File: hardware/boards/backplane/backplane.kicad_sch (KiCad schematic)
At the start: 0 parts

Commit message: Add backplane power connector schematic
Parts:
- added J1: DC_IN_SCREW_TERMINAL, TerminalBlock_Phoenix:TerminalBlock_Phoenix_MKDS-1,5-2-5.08_1x02_P5.08mm_Horizontal, symbol Connector_Generic:Conn_01x02
- added J2: XT30U(2+2)-F.G.B_SLOT1, mini-rack-power:Amass_XT30U_2plus2_F_RightAngle_Mechanical, symbol Connector_Generic:Conn_01x04
- added J3: XT30U(2+2)-F.G.B_SLOT2, mini-rack-power:Amass_XT30U_2plus2_F_RightAngle_Mechanical, symbol Connector_Generic:Conn_01x04
- added J4: XT30U(2+2)-F.G.B_SLOT3, mini-rack-power:Amass_XT30U_2plus2_F_RightAngle_Mechanical, symbol Connector_Generic:Conn_01x04
- added J5: XT30U(2+2)-F.G.B_SLOT4, mini-rack-power:Amass_XT30U_2plus2_F_RightAngle_Mechanical, symbol Connector_Generic:Conn_01x04
- added J6: XT30U(2+2)-F.G.B_SLOT5, mini-rack-power:Amass_XT30U_2plus2_F_RightAngle_Mechanical, symbol Connector_Generic:Conn_01x04
- added J7: XT30U(2+2)-F.G.B_SLOT6, mini-rack-power:Amass_XT30U_2plus2_F_RightAngle_Mechanical, symbol Connector_Generic:Conn_01x04
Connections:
- new net DC_IN+: J1.1 (Pin_1), J2.1 (Pin_1), J3.1 (Pin_1), J4.1 (Pin_1), J5.1 (Pin_1), J6.1 (Pin_1), J7.1 (Pin_1)
- new net GND: J1.2 (Pin_2), J2.2 (Pin_2), J3.2 (Pin_2), J4.2 (Pin_2), J5.2 (Pin_2), J6.2 (Pin_2), J7.2 (Pin_2)
- new net SLOT1_SCL: J2.4 (Pin_4)
- new net SLOT1_SDA: J2.3 (Pin_3)
- new net SLOT2_SCL: J3.4 (Pin_4)
- new net SLOT2_SDA: J3.3 (Pin_3)
- new net SLOT3_SCL: J4.4 (Pin_4)
- new net SLOT3_SDA: J4.3 (Pin_3)
- new net SLOT4_SCL: J5.4 (Pin_4)
- new net SLOT4_SDA: J5.3 (Pin_3)
- new net SLOT5_SCL: J6.4 (Pin_4)
- new net SLOT5_SDA: J6.3 (Pin_3)
- new net SLOT6_SCL: J7.4 (Pin_4)
- new net SLOT6_SDA: J7.3 (Pin_3)
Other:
- note added: "XT30 pin assumption: 1=DC_IN+, 2=GND, 3=SDA, 4=SCL. Verify XT30U female electrical footprint before PCB layout."

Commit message: Checkpoint
_sigh_
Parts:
- added C1: 100nF, Capacitor_SMD:C_0603_1608Metric, symbol Device:C
- added JP1: A0_ADDR, Jumper:SolderJumper-3_P1.3mm_Bridged12_Pad1.0x1.5mm, symbol Jumper:SolderJumper_3_Bridged12
- added JP2: A1_ADDR, Jumper:SolderJumper-3_P1.3mm_Bridged12_Pad1.0x1.5mm, symbol Jumper:SolderJumper_3_Bridged12
- added JP3: A2_ADDR, Jumper:SolderJumper-3_P1.3mm_Bridged12_Pad1.0x1.5mm, symbol Jumper:SolderJumper_3_Bridged12
- added R1: 10k, Resistor_SMD:R_0603_1608Metric, symbol Device:R
- added U1: TCA9548APWR, Package_SO:TSSOP-24_4.4x7.8mm_P0.65mm, symbol Interface_Expansion:TCA9548APWR
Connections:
- net GND: now also C1.2, JP1.1 (A), JP2.1 (A), JP3.1 (A), U1.12 (GND)
- net SLOT1_SCL renamed SCL_SLOT_1
- net SCL_SLOT_1: now also U1.5 (SC0)
- net SLOT1_SDA renamed SDA_SLOT_1
- net SDA_SLOT_1: now also U1.4 (SD0)
- net SLOT2_SCL renamed SCL_SLOT_2
- net SCL_SLOT_2: now also U1.7 (SC1)
- net SLOT2_SDA renamed SDA_SLOT_2
- net SDA_SLOT_2: now also U1.6 (SD1)
- net SLOT3_SCL renamed SCL_SLOT_3
- net SCL_SLOT_3: now also U1.9 (SC2)
- net SLOT3_SDA renamed SDA_SLOT_3
- net SDA_SLOT_3: now also U1.8 (SD2)
- net SLOT4_SCL renamed SCL_SLOT_4
- net SCL_SLOT_4: now also U1.11 (SC3)
- net SLOT4_SDA renamed SDA_SLOT_4
- net SDA_SLOT_4: now also U1.10 (SD3)
- net SLOT5_SCL renamed SCL_SLOT_5
- net SCL_SLOT_5: now also U1.14 (SC4)
- net SLOT5_SDA renamed SDA_SLOT_5
- net SDA_SLOT_5: now also U1.13 (SD4)
- net SLOT6_SCL renamed SCL_SLOT_6
- net SCL_SLOT_6: now also U1.16 (SC5)
- net SLOT6_SDA renamed SDA_SLOT_6
- net SDA_SLOT_6: now also U1.15 (SD5)
- new net: R1.2, U1.3 (~{RESET})
- new net +3V3: C1.1, JP1.3 (B), JP2.3 (B), JP3.3 (B), R1.1, U1.24 (VCC)
- new net I2C_UP_SCL: U1.22 (SCL)
- new net I2C_UP_SDA: U1.23 (SDA)
- new net TCA9548A_A0: JP1.2 (C), U1.1 (A0)
- new net TCA9548A_A1: JP2.2 (C), U1.2 (A1)
- new net TCA9548A_A2: JP3.2 (C), U1.21 (A2)
- no-connect marks 0 -> 4
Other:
- note added: "TCA9548A: JP1-JP3 default A0/A1/A2 low for 0x70; cut 1-2 and bridge 1-3 to set a bit high. VCC_I2C rail and I2C pull-up placement/value still TBD."

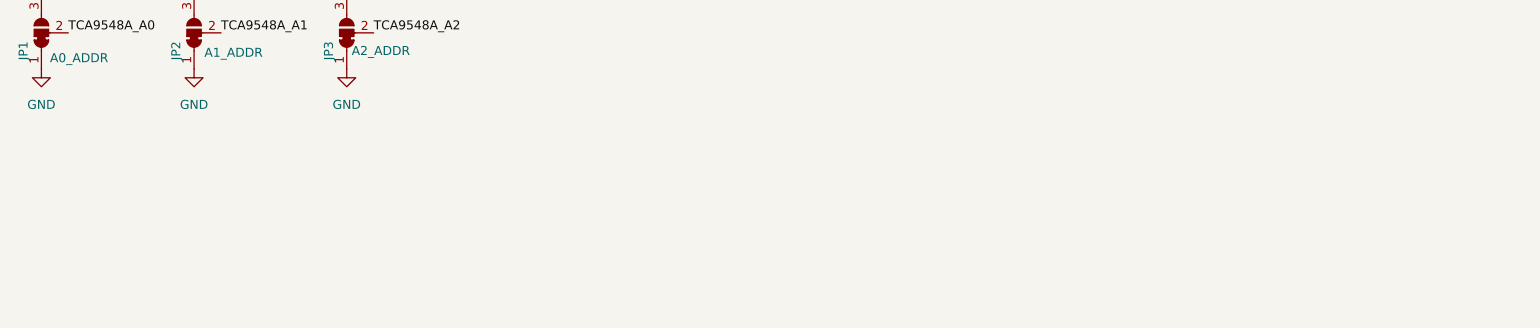
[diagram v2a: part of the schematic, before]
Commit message: Add backplane slot LED indicators
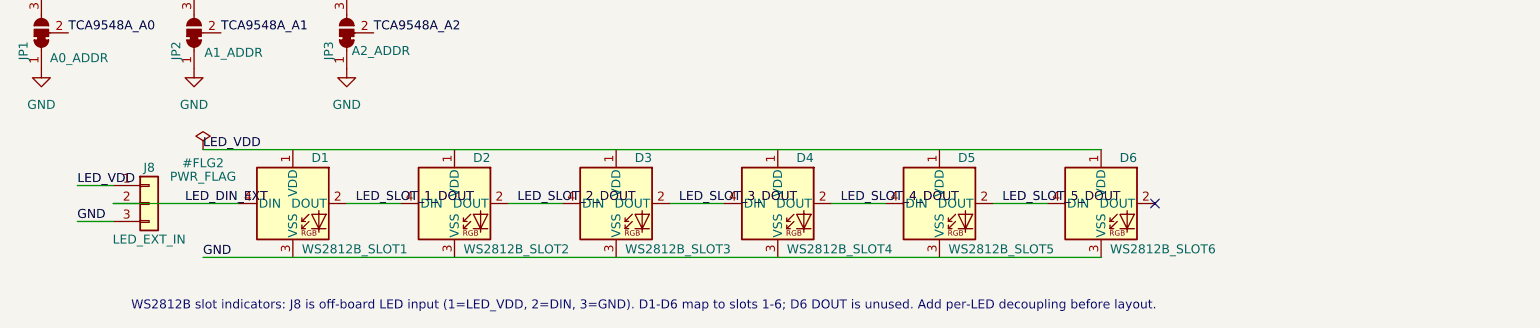
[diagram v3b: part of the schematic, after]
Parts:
- added D1: WS2812B_SLOT1, LED_SMD:LED_WS2812B_PLCC4_5.0x5.0mm_P3.2mm, symbol LED:WS2812B
- added D2: WS2812B_SLOT2, LED_SMD:LED_WS2812B_PLCC4_5.0x5.0mm_P3.2mm, symbol LED:WS2812B
- added D3: WS2812B_SLOT3, LED_SMD:LED_WS2812B_PLCC4_5.0x5.0mm_P3.2mm, symbol LED:WS2812B
- added D4: WS2812B_SLOT4, LED_SMD:LED_WS2812B_PLCC4_5.0x5.0mm_P3.2mm, symbol LED:WS2812B
- added D5: WS2812B_SLOT5, LED_SMD:LED_WS2812B_PLCC4_5.0x5.0mm_P3.2mm, symbol LED:WS2812B
- added D6: WS2812B_SLOT6, LED_SMD:LED_WS2812B_PLCC4_5.0x5.0mm_P3.2mm, symbol LED:WS2812B
- added J8: LED_EXT_IN, Connector_PinHeader_2.54mm:PinHeader_1x03_P2.54mm_Vertical, symbol Connector_Generic:Conn_01x03
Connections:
- net GND: now also D1.3 (VSS), D2.3 (VSS), D3.3 (VSS), D4.3 (VSS), D5.3 (VSS), D6.3 (VSS), J8.3 (Pin_3)
- new net LED_DIN_EXT: D1.4 (DIN), J8.2 (Pin_2)
- new net LED_SLOT_1_DOUT: D1.2 (DOUT), D2.4 (DIN)
- new net LED_SLOT_2_DOUT: D2.2 (DOUT), D3.4 (DIN)
- new net LED_SLOT_3_DOUT: D3.2 (DOUT), D4.4 (DIN)
- new net LED_SLOT_4_DOUT: D4.2 (DOUT), D5.4 (DIN)
- new net LED_SLOT_5_DOUT: D5.2 (DOUT), D6.4 (DIN)
- new net LED_VDD: D1.1 (VDD), D2.1 (VDD), D3.1 (VDD), D4.1 (VDD), D5.1 (VDD), D6.1 (VDD), J8.1 (Pin_1)
- no-connect marks 4 -> 5
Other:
- note added: "WS2812B slot indicators: J8 is off-board LED input (1=LED_VDD, 2=DIN, 3=GND). D1-D6 map to slots 1-6; D6 DOUT is unused. Add per-LED decoupling before layout."

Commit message: Add backplane I2C protection and chaining connectors
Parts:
- added D10, D11, D12, D13, D14, D15, D16, D17, D18, D7, D8, D9: LOW_CAP_TVS, Diode_SMD:D_SOD-523, symbol Device:D_TVS
- added J10: I2C_CHAIN_IN, Connector_PinHeader_2.54mm:PinHeader_1x04_P2.54mm_Vertical, symbol Connector_Generic:Conn_01x04
- added J11: I2C_CHAIN_OUT, Connector_PinHeader_2.54mm:PinHeader_1x04_P2.54mm_Vertical, symbol Connector_Generic:Conn_01x04
- added J12: LED_EXT_OUT, Connector_PinHeader_2.54mm:PinHeader_1x03_P2.54mm_Vertical, symbol Connector_Generic:Conn_01x03
- added J9: DC_CHAIN_OUT, TerminalBlock_Phoenix:TerminalBlock_Phoenix_MKDS-1,5-2-5.08_1x02_P5.08mm_Horizontal, symbol Connector_Generic:Conn_01x02
- added R10, R11, R12, R13, R2, R3, R4, R5, R6, R7, R8, R9: 47R, Resistor_SMD:R_0603_1608Metric, symbol Device:R
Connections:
- net +3V3: now also J10.4 (Pin_4), J11.4 (Pin_4)
- net DC_IN+: now also J9.1 (Pin_1)
- net GND: now also D10.2 (A2), D11.2 (A2), D12.2 (A2), D13.2 (A2), D14.2 (A2), D15.2 (A2), D16.2 (A2), D17.2 (A2), D18.2 (A2), D7.2 (A2), D8.2 (A2), D9.2 (A2), J10.1 (Pin_1), J11.1 (Pin_1), J12.3 (Pin_3), J9.2 (Pin_2)
- net I2C_UP_SCL: now also J10.3 (Pin_3), J11.3 (Pin_3)
- net I2C_UP_SDA: now also J10.2 (Pin_2), J11.2 (Pin_2)
- net LED_VDD: now also J12.1 (Pin_1)
- net SCL_SLOT_1: now also R3.2; no longer J2.4 (Pin_4)
- net SCL_SLOT_2: now also R5.2; no longer J3.4 (Pin_4)
- net SCL_SLOT_3: now also R7.2; no longer J4.4 (Pin_4)
- net SCL_SLOT_4: now also R9.2; no longer J5.4 (Pin_4)
- net SCL_SLOT_5: now also R11.2; no longer J6.4 (Pin_4)
- net SCL_SLOT_6: now also R13.2; no longer J7.4 (Pin_4)
- net SDA_SLOT_1: now also R2.2; no longer J2.3 (Pin_3)
- net SDA_SLOT_2: now also R4.2; no longer J3.3 (Pin_3)
- net SDA_SLOT_3: now also R6.2; no longer J4.3 (Pin_3)
- net SDA_SLOT_4: now also R8.2; no longer J5.3 (Pin_3)
- net SDA_SLOT_5: now also R10.2; no longer J6.3 (Pin_3)
- net SDA_SLOT_6: now also R12.2; no longer J7.3 (Pin_3)
- net LED_DOUT_EXT: now reaches D6.2 (DOUT)
- net LED_DOUT_EXT: now also J12.2 (Pin_2)
- new net SCL_SLOT_1_CONN: D8.1 (A1), J2.4 (Pin_4), R3.1
- new net SCL_SLOT_2_CONN: D10.1 (A1), J3.4 (Pin_4), R5.1
- new net SCL_SLOT_3_CONN: D12.1 (A1), J4.4 (Pin_4), R7.1
- new net SCL_SLOT_4_CONN: D14.1 (A1), J5.4 (Pin_4), R9.1
- new net SCL_SLOT_5_CONN: D16.1 (A1), J6.4 (Pin_4), R11.1
- new net SCL_SLOT_6_CONN: D18.1 (A1), J7.4 (Pin_4), R13.1
- new net SDA_SLOT_1_CONN: D7.1 (A1), J2.3 (Pin_3), R2.1
- new net SDA_SLOT_2_CONN: D9.1 (A1), J3.3 (Pin_3), R4.1
- new net SDA_SLOT_3_CONN: D11.1 (A1), J4.3 (Pin_3), R6.1
- new net SDA_SLOT_4_CONN: D13.1 (A1), J5.3 (Pin_3), R8.1
- new net SDA_SLOT_5_CONN: D15.1 (A1), J6.3 (Pin_3), R10.1
- new net SDA_SLOT_6_CONN: D17.1 (A1), J7.3 (Pin_3), R12.1
- no-connect marks 5 -> 4
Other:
- note added: "Daisy-chain connectors: J9 parallels J1 for DC. J10/J11 parallel the upstream I2C bus as GND/SDA/SCL/+3V3. J12 exports LED_VDD, D6 DOUT, and GND."
- note added: "Per-slot I2C hot-plug protection: R2-R13 are 47R series resistors. D7-D18 are low-cap TVS placeholders from connector-side nets to GND; final TVS capacitance/clamp TBD."
- note added: "WS2812B slot indicators: J8 is off-board LED input (1=LED_VDD, 2=DIN, 3=GND). D1-D6 map to slots 1-6; J12 exports D6 DOUT for daisy-chain output. Add per-LED decoupling before layout."
- note removed: "WS2812B slot indicators: J8 is off-board LED input (1=LED_VDD, 2=DIN, 3=GND). D1-D6 map to slots 1-6; D6 DOUT is unused. Add per-LED decoupling before layout."

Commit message: chore: add placeholder part source properties
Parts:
- C1, D1, D10, D11, D12, D13, D14, D15, D16, D17, D18, D2, D3, D4, D5, D6, D7, D8, D9, J1, J10, J11, J12, J2, J3, J4, J5, J6, J7, J8, J9, JP1, JP2, JP3, R1, R10, R11, R12, R13, R2, R3, R4, R5, R6, R7, R8, R9, U1: Part_source (none) -> LCSC,XXXXXXX

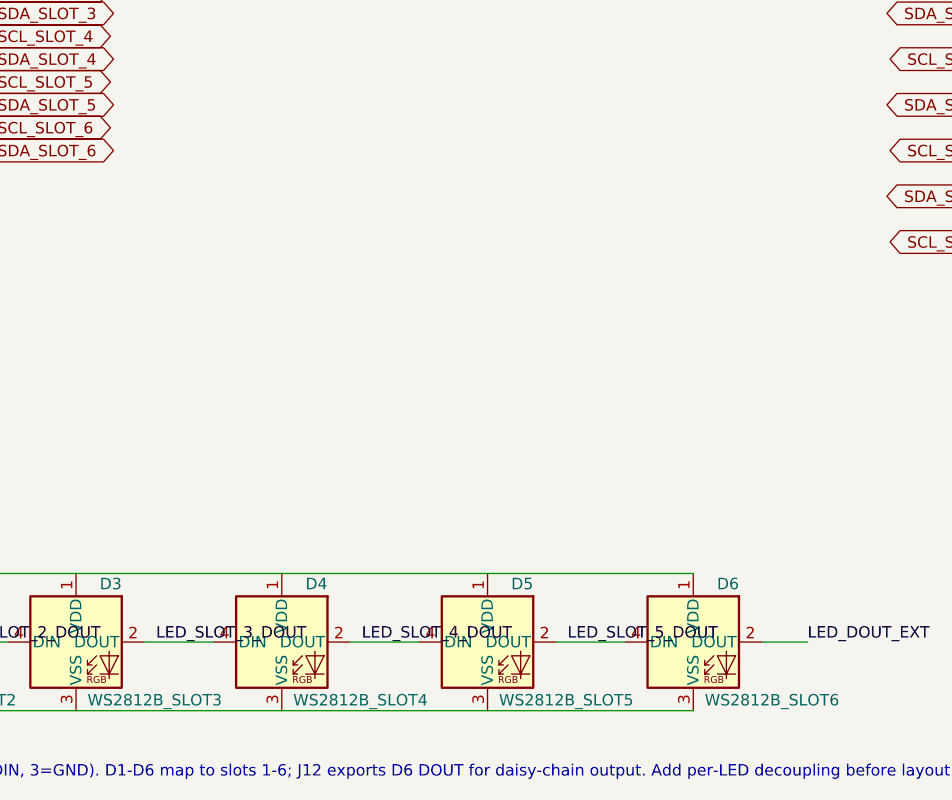
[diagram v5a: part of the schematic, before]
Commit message: add wt32 eth01 backplane module
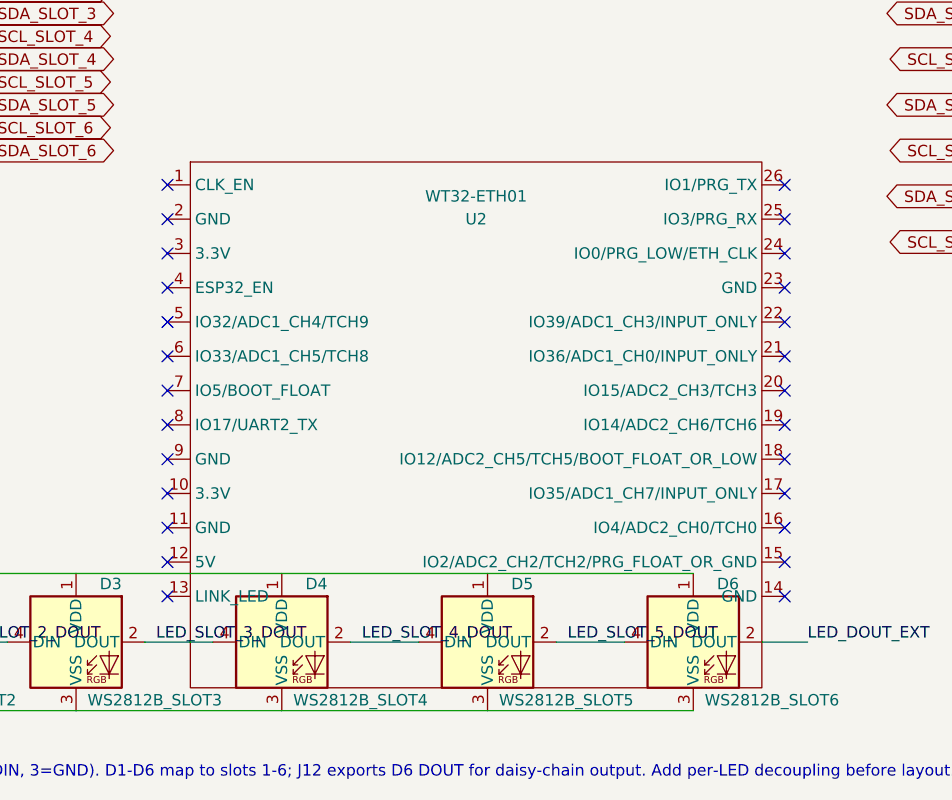
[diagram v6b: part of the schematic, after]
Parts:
- added U2: WT32-ETH01, WT32-ETH01:WT32-ETH01, symbol WT32-ETH01:WT32-ETH01
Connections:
- no-connect marks 4 -> 30
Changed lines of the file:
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@@
+		)
+	)
+	(no_connect
+		(at 114.30 151.13)
+	)
+	(no_connect
+		(at 114.30 185.42)
+	)
+	(no_connect
+		(at 114.30 189.23)
+	)
+	(no_connect
+		(at 114.30 193.04)
+	)
+	(no_connect
+		(at 114.30 196.85)
+	)
+	(no_connect
+		(at 182.88 196.85)
+	)
+	(no_connect
+		(at 182.88 193.04)
+	)
+	(no_connect
+		(at 182.88 189.23)
+	)
+	(no_connect
+		(at 182.88 185.42)
+	)
+	(no_connect
+		(at 182.88 181.61)
+	)
+	(no_connect
+		(at 182.88 177.80)
+	)
+	(no_connect
+		(at 114.30 154.94)
+	)
+	(no_connect
+		(at 182.88 173.99)
+	)
+	(no_connect
+		(at 182.88 170.18)
+	)
+	(no_connect
+		(at 182.88 166.37)
+	)
+	(no_connect
+		(at 182.88 162.56)
+	)
+	(no_connect
+		(at 182.88 158.75)
+	)
+	(no_connect
+		(at 182.88 154.94)
+	)
+	(no_connect
+		(at 182.88 151.13)
+	)
+	(no_connect
+		(at 114.30 158.75)
+	)
+	(no_connect
+		(at 114.30 162.56)
+	)
+	(no_connect
+		(at 114.30 166.37)
+	)
+	(no_connect
+		(at 114.30 170.18)
+	)
+	(no_connect
+		(at 114.30 173.99)
+	)
+	(no_connect
+		(at 114.30 177.80)
+	)
+	(no_connect
+		(at 114.30 181.61)
+	)
+	(symbol
+		(lib_id "WT32-ETH01:WT32-ETH01")
+		(at 148.59 177.80 0)
+		(unit 1)
+		(body_style 1)
+		(exclude_from_sim no)
+		(in_bom yes)
+		(on_board yes)
+		(in_pos_files yes)
+		(dnp no)
+		(property "Reference" "U2"
+			(at 148.59 154.94 0)
+			(show_name no)
+			(do_not_autoplace no)
+			(effects
+				(font
+					(size 1.27 1.27)
+				)
+			)
+		)
+		(property "Value" "WT32-ETH01"
+			(at 148.59 152.40 0)
+			(show_name no)
+			(do_not_autoplace no)
+			(effects
+				(font
+					(size 1.27 1.27)
+				)
+			)
+		)
+		(property "Footprint" "WT32-ETH01:WT32-ETH01"
+			(at 148.59 177.80 0)
+			(hide yes)
+			(show_name no)
+			(do_not_autoplace no)
+			(effects
+				(font
+					(size 1.27 1.27)
+				)
+			)
+		)
+		(property "Datasheet" "${KIPRJMOD}/../../libraries/vendor/wt32-eth01/WT32-ETH01-datasheet-v1.4-en.pdf"
+			(at 148.59 177.80 0)
+			(hide yes)
+			(show_name no)
+			(do_not_autoplace no)
+			(effects
+				(font
+					(size 1.27 1.27)
+				)
+			)
+		)
+		(property "Description" "WT32-ETH01 ESP32 Ethernet module"
+			(at 148.59 177.80 0)
+			(hide yes)
+			(show_name no)
+			(do_not_autoplace no)
+			(effects
+				(font
+					(size 1.27 1.27)
+				)
+			)
+		)
+		(property "Part_source" "LCSC,XXXXXXX"
+			(at 148.59 177.80 0)
+			(hide yes)
+			(show_name no)
+			(do_not_autoplace no)
+			(effects
+				(font
+					(size 1.27 1.27)
+				)
+			)
+		)
+		(pin "1"
+		)
+		(pin "10"
+		)
+		(pin "11"
+		)
+		(pin "12"
+		)
+		(pin "13"
+		)
+		(pin "14"
+		)
+		(pin "15"
+		)
+		(pin "16"
+		)
+		(pin "17"
+		)
+		(pin "18"
+		)
+		(pin "19"
+		)
+		(pin "2"
+		)
+		(pin "20"
+		)
+		(pin "21"
+		)
+		(pin "22"
+		)
+		(pin "23"
+		)
+		(pin "24"
+		)
+		(pin "25"
+		)
+		(pin "26"
+		)
+		(pin "3"
+		)
+		(pin "4"
+		)
+		(pin "5"
+		)
+		(pin "6"
+		)
+		(pin "7"
+		)
+		(pin "8"
+		)
+		(pin "9"
+		)
+		(instances
+			(project "backplane"
+				(path "/5e4f3adc-13b5-4625-8ac7-2a60909b6ea0"
+					(reference "U2")
+					(unit 1)
+				)
+			)
 		)
 	)

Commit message: Split backplane schematic pages
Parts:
- removed C1: 100nF, Capacitor_SMD:C_0603_1608Metric, symbol Device:C
- removed D1: WS2812B_SLOT1, LED_SMD:LED_WS2812B_PLCC4_5.0x5.0mm_P3.2mm, symbol LED:WS2812B
- removed D10, D11, D12, D13, D14, D15, D16, D17, D18, D7, D8, D9: LOW_CAP_TVS, Diode_SMD:D_SOD-523, symbol Device:D_TVS
- removed D2: WS2812B_SLOT2, LED_SMD:LED_WS2812B_PLCC4_5.0x5.0mm_P3.2mm, symbol LED:WS2812B
- removed D3: WS2812B_SLOT3, LED_SMD:LED_WS2812B_PLCC4_5.0x5.0mm_P3.2mm, symbol LED:WS2812B
- removed D4: WS2812B_SLOT4, LED_SMD:LED_WS2812B_PLCC4_5.0x5.0mm_P3.2mm, symbol LED:WS2812B
- removed D5: WS2812B_SLOT5, LED_SMD:LED_WS2812B_PLCC4_5.0x5.0mm_P3.2mm, symbol LED:WS2812B
- removed D6: WS2812B_SLOT6, LED_SMD:LED_WS2812B_PLCC4_5.0x5.0mm_P3.2mm, symbol LED:WS2812B
- removed J1: DC_IN_SCREW_TERMINAL, TerminalBlock_Phoenix:TerminalBlock_Phoenix_MKDS-1,5-2-5.08_1x02_P5.08mm_Horizontal, symbol Connector_Generic:Conn_01x02
- removed J10: I2C_CHAIN_IN, Connector_PinHeader_2.54mm:PinHeader_1x04_P2.54mm_Vertical, symbol Connector_Generic:Conn_01x04
- removed J11: I2C_CHAIN_OUT, Connector_PinHeader_2.54mm:PinHeader_1x04_P2.54mm_Vertical, symbol Connector_Generic:Conn_01x04
- removed J12: LED_EXT_OUT, Connector_PinHeader_2.54mm:PinHeader_1x03_P2.54mm_Vertical, symbol Connector_Generic:Conn_01x03
- removed J2: XT30U(2+2)-F.G.B_SLOT1, mini-rack-power:Amass_XT30U_2plus2_F_RightAngle_Mechanical, symbol Connector_Generic:Conn_01x04
- removed J3: XT30U(2+2)-F.G.B_SLOT2, mini-rack-power:Amass_XT30U_2plus2_F_RightAngle_Mechanical, symbol Connector_Generic:Conn_01x04
- removed J4: XT30U(2+2)-F.G.B_SLOT3, mini-rack-power:Amass_XT30U_2plus2_F_RightAngle_Mechanical, symbol Connector_Generic:Conn_01x04
- removed J5: XT30U(2+2)-F.G.B_SLOT4, mini-rack-power:Amass_XT30U_2plus2_F_RightAngle_Mechanical, symbol Connector_Generic:Conn_01x04
- removed J6: XT30U(2+2)-F.G.B_SLOT5, mini-rack-power:Amass_XT30U_2plus2_F_RightAngle_Mechanical, symbol Connector_Generic:Conn_01x04
- removed J7: XT30U(2+2)-F.G.B_SLOT6, mini-rack-power:Amass_XT30U_2plus2_F_RightAngle_Mechanical, symbol Connector_Generic:Conn_01x04
- removed J8: LED_EXT_IN, Connector_PinHeader_2.54mm:PinHeader_1x03_P2.54mm_Vertical, symbol Connector_Generic:Conn_01x03
- removed J9: DC_CHAIN_OUT, TerminalBlock_Phoenix:TerminalBlock_Phoenix_MKDS-1,5-2-5.08_1x02_P5.08mm_Horizontal, symbol Connector_Generic:Conn_01x02
- removed JP1: A0_ADDR, Jumper:SolderJumper-3_P1.3mm_Bridged12_Pad1.0x1.5mm, symbol Jumper:SolderJumper_3_Bridged12
- removed JP2: A1_ADDR, Jumper:SolderJumper-3_P1.3mm_Bridged12_Pad1.0x1.5mm, symbol Jumper:SolderJumper_3_Bridged12
- removed JP3: A2_ADDR, Jumper:SolderJumper-3_P1.3mm_Bridged12_Pad1.0x1.5mm, symbol Jumper:SolderJumper_3_Bridged12
- removed R1: 10k, Resistor_SMD:R_0603_1608Metric, symbol Device:R
- removed R10, R11, R12, R13, R2, R3, R4, R5, R6, R7, R8, R9: 47R, Resistor_SMD:R_0603_1608Metric, symbol Device:R
- removed U1: TCA9548APWR, Package_SO:TSSOP-24_4.4x7.8mm_P0.65mm, symbol Interface_Expansion:TCA9548APWR
- removed U2: WT32-ETH01, WT32-ETH01:WT32-ETH01, symbol WT32-ETH01:WT32-ETH01
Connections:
- no-connect marks 30 -> 0
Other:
- added sheet Control and Fan (backplane_control_fan.kicad_sch)
- added sheet Slots and LEDs (backplane_slots_leds.kicad_sch)
- note removed: "Daisy-chain connectors: J9 parallels J1 for DC. J10/J11 parallel the upstream I2C bus as GND/SDA/SCL/+3V3. J12 exports LED_VDD, D6 DOUT, and GND."
- note removed: "Per-slot I2C hot-plug protection: R2-R13 are 47R series resistors. D7-D18 are low-cap TVS placeholders from connector-side nets to GND; final TVS capacitance/clamp TBD."
- note removed: "TCA9548A: JP1-JP3 default A0/A1/A2 low for 0x70; cut 1-2 and bridge 1-3 to set a bit high. VCC_I2C rail and I2C pull-up placement/value still TBD."
- note removed: "WS2812B slot indicators: J8 is off-board LED input (1=LED_VDD, 2=DIN, 3=GND). D1-D6 map to slots 1-6; J12 exports D6 DOUT for daisy-chain output. Add per-LED decoupling before layout."
- note removed: "XT30 pin assumption: 1=DC_IN+, 2=GND, 3=SDA, 4=SCL. Verify XT30U female electrical footprint before PCB layout."
